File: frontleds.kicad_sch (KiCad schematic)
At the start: 2 parts

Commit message: finished adding front leds
probably works idk
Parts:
- D11, D12: footprint LED_SMD:LED_SK6812_PLCC4_5.0x5.0mm_P3.2mm -> LED_SMD:LED_SK6812B_SIDE_4.0mmx1.5mm
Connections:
- net +5V: now also D11.2 (VDD), D12.2 (VDD); no longer D11.3 (VDD), D12.3 (VDD)
- net GND: now also D11.4 (GND), D12.4 (GND); no longer D11.1 (VSS), D12.1 (VSS)
- net GPIO12: now also D11.1 (DIN); no longer D11.2 (DIN)
- new net: D11.3 (DOUT), D12.1 (DIN)
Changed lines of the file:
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@@
+	)
+	(symbol
+		(lib_id "LED:SK6812B")
+		(at 55.88 29.21 0)
+		(unit 1)
+		(exclude_from_sim no)
+		(in_bom yes)
+		(on_board yes)
+		(dnp no)
+		(fields_autoplaced yes)
+		(property "Reference" "D12"
+			(at 66.04 22.7898 0)
+			(effects
+				(font
+					(size 1.27 1.27)
+				)
+			)
+		)
+		(property "Value" "SK6812B"
+			(at 66.04 25.3298 0)
+			(effects
+				(font
+					(size 1.27 1.27)
+				)
+			)
+		)
+		(property "Footprint" "LED_SMD:LED_SK6812B_SIDE_4.0mmx1.5mm"
+			(at 55.88 29.21 0)
+			(effects
+				(font
+					(size 1.27 1.27)
+				)
+				(hide yes)
+			)
+		)
+		(property "Datasheet" "https://core-electronics.com.au/attachments/localcontent/4691_SK68XX_SIDE_REV_55747b5a68c.pdf"
+			(at 55.88 10.16 0)
+			(effects
+				(font
+					(size 1.27 1.27)
+				)
+				(hide yes)
+			)
+		)
+		(property "Description" "RGB LED with integrated controller"
+			(at 55.88 7.62 0)
+			(effects
+				(font
+					(size 1.27 1.27)
+				)
+				(hide yes)
+			)
+		)
+		(pin "3"
+		)
+		(pin "1"
+		)
+		(pin "4"
+		)
+		(pin "2"
+		)
+		(instances
+			(project "robot_pcb"
+				(path "/2f56b371-1597-47e1-a48d-b7f69d342f77/f9fd353d-136c-4b1d-af31-404dc5242855"
+					(reference "D12")
+					(unit 1)
+				)
+			)
+		)
 	)
 	(symbol
@@
 	)
 	(symbol
+		(lib_id "power:GND")
+		(at 41.91 39.37 0)
+		(unit 1)
+		(exclude_from_sim no)
+		(in_bom yes)
+		(on_board yes)
+		(dnp no)
+		(fields_autoplaced yes)
+		(property "Reference" "#PWR0121"
+			(at 41.91 45.72 0)
+			(effects
+				(font
+					(size 1.27 1.27)
+				)
+				(hide yes)
+			)
+		)
+		(property "Value" "GND"
+			(at 41.91 44.45 0)
+			(effects
+				(font
+					(size 1.27 1.27)
+				)
+			)
+		)
+		(property "Footprint" ""
+			(at 41.91 39.37 0)
+			(effects
+				(font
+					(size 1.27 1.27)
+				)
+				(hide yes)
+			)
+		)
+		(property "Datasheet" ""
+			(at 41.91 39.37 0)
+			(effects
+				(font
+					(size 1.27 1.27)
+				)
+				(hide yes)
+			)
+		)
+		(property "Description" "Power symbol creates a global label with name \"GND\" , ground"
+			(at 41.91 39.37 0)
+			(effects
+				(font
+					(size 1.27 1.27)
+				)
+				(hide yes)
+			)
+		)
+		(pin "1"
+		)
+		(instances
+			(project ""
+				(path "/2f56b371-1597-47e1-a48d-b7f69d342f77/f9fd353d-136c-4b1d-af31-404dc5242855"
+					(reference "#PWR0121")
+					(unit 1)
+				)
+			)
+		)
+	)
+	(symbol
 		(lib_id "LED:SK6812B")
 		(at 29.21 29.21 0)
@@
 		(fields_autoplaced yes)
 		(property "Reference" "D11"
-			(at 40.64 22.7898 0)
+			(at 39.37 22.7898 0)
 			(effects
 				(font
@@
 		)
 		(property "Value" "SK6812B"
-			(at 40.64 25.3298 0)
-			(effects
-				(font
-					(size 1.27 1.27)
-				)
-			)
-		)
-		(property "Footprint" "LED_SMD:LED_SK6812_PLCC4_5.0x5.0mm_P3.2mm"
-			(at 30.48 36.83 0)
-			(effects
-				(font
-					(size 1.27 1.27)
-				)
-				(justify left top)
+			(at 39.37 25.3298 0)
+			(effects
+				(font
+					(size 1.27 1.27)
+				)
+			)
+		)
+		(property "Footprint" "LED_SMD:LED_SK6812B_SIDE_4.0mmx1.5mm"
+			(at 29.21 29.21 0)
+			(effects
+				(font
+					(size 1.27 1.27)
+				)
 				(hide yes)
 			)
 		)
 		(property "Datasheet" "https://core-electronics.com.au/attachments/localcontent/4691_SK68XX_SIDE_REV_55747b5a68c.pdf"
-			(at 31.75 38.735 0)
-			(effects
-				(font
-					(size 1.27 1.27)
-				)
-				(justify left top)
-				(hide yes)
-			)
-		)
-		(property "Description" "Side-light RGB LED with integrated controller"
-			(at 29.21 29.21 0)
-			(effects
-				(font
-					(size 1.27 1.27)
-				)
-				(hide yes)
-			)
+			(at 29.21 10.16 0)
+			(effects
+				(font
+					(size 1.27 1.27)
+				)
+				(hide yes)
+			)
+		)
+		(property "Description" "RGB LED with integrated controller"
+			(at 29.21 7.62 0)
+			(effects
+				(font
+					(size 1.27 1.27)
+				)
+				(hide yes)
+			)
+		)
+		(pin "3"
+		)
+		(pin "1"
+		)
+		(pin "4"
 		)
 		(pin "2"
 		)
-		(pin "1"
-		)
-		(pin "4"
-		)
-		(pin "3"
-		)
 		(instances
 			(project ""
@@
 					(unit 1)
 				)
-			)
-		)
-	)
-	(symbol
-		(lib_id "power:GND")
-		(at 41.91 39.37 0)
-		(unit 1)
-		(exclude_from_sim no)
-		(in_bom yes)
-		(on_board yes)
-		(dnp no)
-		(fields_autoplaced yes)
-		(property "Reference" "#PWR0121"
-			(at 41.91 45.72 0)
-			(effects
-				(font
-					(size 1.27 1.27)
-				)
-				(hide yes)
-			)
-		)
-		(property "Value" "GND"
-			(at 41.91 44.45 0)
-			(effects
-				(font
-					(size 1.27 1.27)
-				)
-			)
-		)
-		(property "Footprint" ""
-			(at 41.91 39.37 0)
-			(effects
-				(font
-					(size 1.27 1.27)
-				)
-				(hide yes)
-			)
-		)
-		(property "Datasheet" ""
-			(at 41.91 39.37 0)
-			(effects
-				(font
-					(size 1.27 1.27)
-				)
-				(hide yes)
-			)
-		)
-		(property "Description" "Power symbol creates a global label with name \"GND\" , ground"
-			(at 41.91 39.37 0)
-			(effects
-				(font
-					(size 1.27 1.27)
-				)
-				(hide yes)
-			)
-		)
-		(pin "1"
-		)
-		(instances
-			(project ""
-				(path "/2f56b371-1597-47e1-a48d-b7f69d342f77/f9fd353d-136c-4b1d-af31-404dc5242855"
-					(reference "#PWR0121")
-					(unit 1)
-				)
-			)
-		)
-	)
-	(symbol
-		(lib_id "LED:SK6812B")
-		(at 55.88 29.21 0)
-		(unit 1)
-		(exclude_from_sim no)
-		(in_bom yes)
-		(on_board yes)
-		(dnp no)
-		(fields_autoplaced yes)
-		(property "Reference" "D12"
-			(at 67.31 22.7898 0)
-			(effects
-				(font
-					(size 1.27 1.27)
-				)
-			)
-		)
-		(property "Value" "SK6812B"
-			(at 67.31 25.3298 0)
-			(effects
-				(font
-					(size 1.27 1.27)
-				)
-			)
-		)
-		(property "Footprint" "LED_SMD:LED_SK6812_PLCC4_5.0x5.0mm_P3.2mm"
-			(at 57.15 36.83 0)
-			(effects
-				(font
-					(size 1.27 1.27)
-				)
-				(justify left top)
-				(hide yes)
-			)
-		)
-		(property "Datasheet" "https://core-electronics.com.au/attachments/localcontent/4691_SK68XX_SIDE_REV_55747b5a68c.pdf"
-			(at 58.42 38.735 0)
-			(effects
-				(font
-					(size 1.27 1.27)
-				)
-				(justify left top)
-				(hide yes)
-			)
-		)
-		(property "Description" "Side-light RGB LED with integrated controller"
-			(at 55.88 29.21 0)
-			(effects
-				(font
-					(size 1.27 1.27)
-				)
-				(hide yes)
-			)
-		)
-		(pin "2"
-		)
-		(pin "1"
-		)
-		(pin "4"
-		)
-		(pin "3"
-		)
-		(instances
-			(project "robot_pcb"
-				(path "/2f56b371-1597-47e1-a48d-b7f69d342f77/f9fd353d-136c-4b1d-af31-404dc5242855"
-					(reference "D12")
-					(unit 1)
-				)

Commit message: send help
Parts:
- removed D11, D12: SK6812B, LED_SMD:LED_SK6812B_SIDE_4.0mmx1.5mm, symbol LED:SK6812B
- added J12, J13: Conn_01x02_Socket, Connector:JWT_A3963_1x02_P3.96mm_Vertical, symbol Connector:Conn_01x02_Socket
- added R54, R55: 8, Resistor_SMD:R_0402_1005Metric, symbol Device:R
- added U18: DMG2305UX-7, Package_TO_SOT_SMD:TSOT-23, symbol Transistor_FET:DMG2305UX-7
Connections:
- net GND: now also J12.2 (Pin_2), J13.2 (Pin_2)
- net GPIO12: now also U18.1 (G)
- new net: R54.1, R55.1
- new net +12V: U18.2 (S)
- new net LED1: J12.1 (Pin_1), R54.2
- new net LED2: J13.1 (Pin_1), R55.2
- no-connect marks 1 -> 0

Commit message: more stuff with switches n things
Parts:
- R54, R55: value 8 -> 10
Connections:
- net at R54.1, R55.1: now also U18.3 (D)
- net LED1: no longer names the net of J12.1 (Pin_1), R54.2
- net LED2: no longer names the net of J13.1 (Pin_1), R55.2
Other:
- moved on the sheet: J12, J13, R54, R55, U18

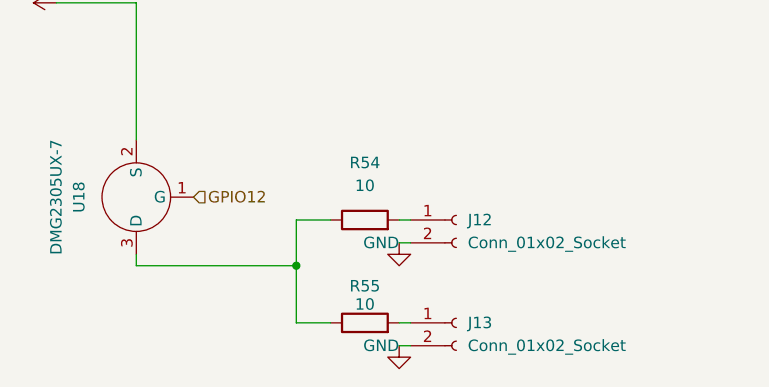
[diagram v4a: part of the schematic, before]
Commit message: added labels to everything
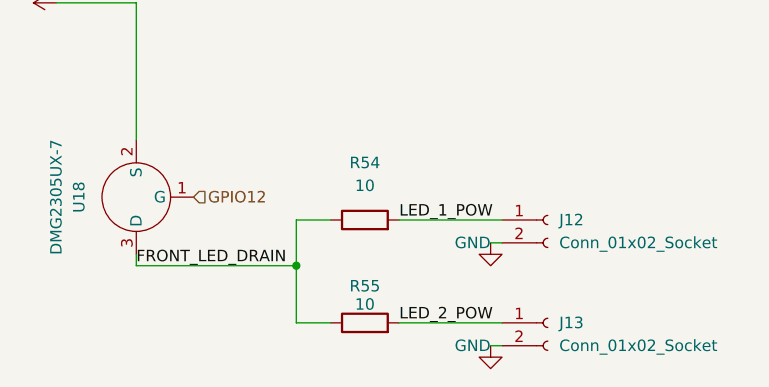
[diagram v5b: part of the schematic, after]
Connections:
- net FRONT_LED_DRAIN: now reaches R54.1, R55.1, U18.3 (D)
- net LED_1_POW: now reaches J12.1 (Pin_1), R54.2
- net LED_2_POW: now reaches J13.1 (Pin_1), R55.2
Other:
- moved on the sheet: J12, J13
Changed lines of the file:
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@@
 	(wire
 		(pts
-			(xy 82.55 63.5) (xy 83.82 63.5)
-		)
-		(stroke
-			(width 0)
-			(type default)
-		)
-	)
-	(wire
-		(pts
-			(xy 82.55 60.96) (xy 83.82 60.96)
+			(xy 92.71 63.5) (xy 93.98 63.5)
 		)
 		(stroke
@@
 	(wire
 		(pts
-			(xy 82.55 52.07) (xy 83.82 52.07)
+			(xy 82.55 60.96) (xy 93.98 60.96)
+		)
+		(stroke
+			(width 0)
+			(type default)
+		)
+	)
+	(wire
+		(pts
+			(xy 92.71 52.07) (xy 93.98 52.07)
 		)
 		(stroke
@@
 	(wire
 		(pts
-			(xy 82.55 49.53) (xy 83.82 49.53)
+			(xy 82.55 49.53) (xy 93.98 49.53)
 		)
 		(stroke
@@
 			(width 0)
 			(type default)
+		)
+	)
+	(label "LED_2_POW"
+		(at 82.55 60.96 0)
+		(effects
+			(font
+				(size 1.27 1.27)
+			)
+			(justify left bottom)
+		)
+	)
+	(label "FRONT_LED_DRAIN"
+		(at 53.34 54.61 0)
+		(effects
+			(font
+				(size 1.27 1.27)
+			)
+			(justify left bottom)
+		)
+	)
+	(label "LED_1_POW"
+		(at 82.55 49.53 0)
+		(effects
+			(font
+				(size 1.27 1.27)
+			)
+			(justify left bottom)
 		)
 	)
@@
 	(symbol
 		(lib_id "power:GND")
-		(at 82.55 63.5 0)
+		(at 92.71 63.5 0)
 		(unit 1)
 		(exclude_from_sim no)
@@
 		(dnp no)
 		(property "Reference" "#PWR0124"
-			(at 82.55 69.85 0)
+			(at 92.71 69.85 0)
 			(effects
 				(font
@@
 		)
 		(property "Value" "GND"
-			(at 82.55 63.5 0)
+			(at 92.71 63.5 0)
 			(effects
 				(font
@@
 		)
 		(property "Footprint" ""
-			(at 82.55 63.5 0)
+			(at 92.71 63.5 0)
 			(effects
 				(font
@@
 		)
 		(property "Datasheet" ""
-			(at 82.55 63.5 0)
+			(at 92.71 63.5 0)
 			(effects
 				(font
@@
 		)
 		(property "Description" "Power symbol creates a global label with name \"GND\" , ground"
-			(at 82.55 63.5 0)
+			(at 92.71 63.5 0)
 			(effects
 				(font
@@
 	(symbol
 		(lib_id "Connector:Conn_01x02_Socket")
-		(at 88.9 49.53 0)
+		(at 99.06 49.53 0)
 		(unit 1)
 		(exclude_from_sim no)
@@
 		(fields_autoplaced yes)
 		(property "Reference" "J12"
-			(at 90.17 49.5299 0)
+			(at 100.33 49.5299 0)
 			(effects
 				(font
@@
 		)
 		(property "Value" "Conn_01x02_Socket"
-			(at 90.17 52.0699 0)
+			(at 100.33 52.0699 0)
 			(effects
 				(font
@@
 		)
 		(property "Footprint" "Connector:JWT_A3963_1x02_P3.96mm_Vertical"
-			(at 88.9 49.53 0)
+			(at 99.06 49.53 0)
 			(effects
 				(font
@@
 		)
 		(property "Datasheet" "~"
-			(at 88.9 49.53 0)
+			(at 99.06 49.53 0)
 			(effects
 				(font
@@
 		)
 		(property "Description" "Generic connector, single row, 01x02, script generated"
-			(at 88.9 49.53 0)
+			(at 99.06 49.53 0)
 			(effects
 				(font
@@
 	(symbol
 		(lib_id "power:GND")
-		(at 82.55 52.07 0)
+		(at 92.71 52.07 0)
 		(unit 1)
 		(exclude_from_sim no)
@@
 		(dnp no)
 		(property "Reference" "#PWR0121"
-			(at 82.55 58.42 0)
+			(at 92.71 58.42 0)
 			(effects
 				(font
@@
 		)
 		(property "Value" "GND"
-			(at 82.55 52.07 0)
+			(at 92.71 52.07 0)
 			(effects
 				(font
@@
 		)
 		(property "Footprint" ""
-			(at 82.55 52.07 0)
+			(at 92.71 52.07 0)
 			(effects
 				(font
@@
 		)
 		(property "Datasheet" ""
-			(at 82.55 52.07 0)
+			(at 92.71 52.07 0)
 			(effects
 				(font
@@
 		)
 		(property "Description" "Power symbol creates a global label with name \"GND\" , ground"
-			(at 82.55 52.07 0)
+			(at 92.71 52.07 0)
 			(effects
 				(font
@@
 	(symbol
 		(lib_id "Connector:Conn_01x02_Socket")
-		(at 88.9 60.96 0)
+		(at 99.06 60.96 0)
 		(unit 1)
 		(exclude_from_sim no)
@@
 		(fields_autoplaced yes)
 		(property "Reference" "J13"
-			(at 90.17 60.9599 0)
+			(at 100.33 60.9599 0)
 			(effects
 				(font
@@
 		)
 		(property "Value" "Conn_01x02_Socket"
-			(at 90.17 63.4999 0)
+			(at 100.33 63.4999 0)
 			(effects
 				(font
@@
 		)
 		(property "Footprint" "Connector:JWT_A3963_1x02_P3.96mm_Vertical"
-			(at 88.9 60.96 0)
+			(at 99.06 60.96 0)
 			(effects
 				(font
@@
 		)
 		(property "Datasheet" "~"
-			(at 88.9 60.96 0)
+			(at 99.06 60.96 0)
 			(effects
 				(font
@@
 		)
 		(property "Description" "Generic connector, single row, 01x02, script generated"
-			(at 88.9 60.96 0)
-			(effects
-				(font
+			(at 99.06 60.96 0)
+			(effects
+				(font

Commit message: more lcsc part labels for non generic components
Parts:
- U18: LCSC (none) -> C150470
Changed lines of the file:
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@@
 			)
 		)
-		(property "LCSC" ""
+		(property "LCSC" "C150470"
 			(at 53.34 46.99 90)
 			(effects

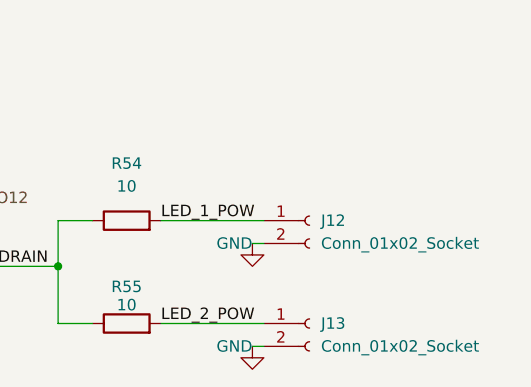
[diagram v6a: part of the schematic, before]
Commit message: Updated edge cuts and drawings from earlier fusion changes and moved traces accordingly
Also fixed jst connectors
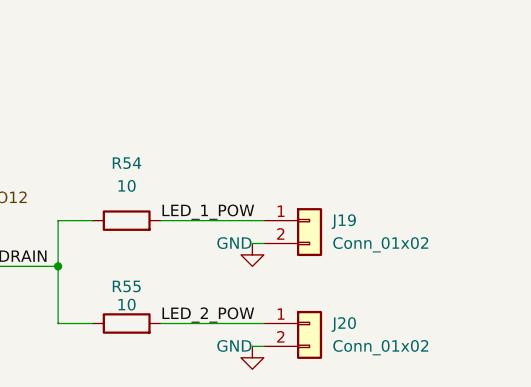
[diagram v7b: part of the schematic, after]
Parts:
- removed J12, J13: Conn_01x02_Socket, Connector:JWT_A3963_1x02_P3.96mm_Vertical, symbol Connector:Conn_01x02_Socket
- added J19, J20: Conn_01x02, Connector_JST:JST_PH_B2B-PH-K_1x02_P2.00mm_Vertical, symbol Connector_Generic:Conn_01x02
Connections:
- net GND: now also J19.2 (Pin_2), J20.2 (Pin_2)
- net LED_1_POW: now also J19.1 (Pin_1)
- net LED_2_POW: now also J20.1 (Pin_1)
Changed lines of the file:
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@@
-	)
-	(symbol
-		(lib_id "Connector:Conn_01x02_Socket")
-		(at 99.06 49.53 0)
-		(unit 1)
-		(exclude_from_sim no)
-		(in_bom yes)
-		(on_board yes)
-		(dnp no)
-		(fields_autoplaced yes)
-		(property "Reference" "J12"
-			(at 100.33 49.5299 0)
-			(effects
-				(font
-					(size 1.27 1.27)
-				)
-				(justify left)
-			)
-		)
-		(property "Value" "Conn_01x02_Socket"
-			(at 100.33 52.0699 0)
-			(effects
-				(font
-					(size 1.27 1.27)
-				)
-				(justify left)
-			)
-		)
-		(property "Footprint" "Connector:JWT_A3963_1x02_P3.96mm_Vertical"
-			(at 99.06 49.53 0)
-			(effects
-				(font
-					(size 1.27 1.27)
-				)
-				(hide yes)
-			)
-		)
-		(property "Datasheet" "~"
-			(at 99.06 49.53 0)
-			(effects
-				(font
-					(size 1.27 1.27)
-				)
-				(hide yes)
-			)
-		)
-		(property "Description" "Generic connector, single row, 01x02, script generated"
-			(at 99.06 49.53 0)
-			(effects
-				(font
-					(size 1.27 1.27)
-				)
-				(hide yes)
-			)
-		)
-		(pin "2"
-		)
-		(pin "1"
-		)
-		(instances
-			(project ""
-				(path "/2f56b371-1597-47e1-a48d-b7f69d342f77/f9fd353d-136c-4b1d-af31-404dc5242855"
-					(reference "J12")
-					(unit 1)
-				)
-			)
-		)
 	)
 	(symbol
@@
 				(path "/2f56b371-1597-47e1-a48d-b7f69d342f77/f9fd353d-136c-4b1d-af31-404dc5242855"
 					(reference "#PWR0121")
-					(unit 1)
-				)
-			)
-		)
-	)
-	(symbol
-		(lib_id "Connector:Conn_01x02_Socket")
-		(at 99.06 60.96 0)
-		(unit 1)
-		(exclude_from_sim no)
-		(in_bom yes)
-		(on_board yes)
-		(dnp no)
-		(fields_autoplaced yes)
-		(property "Reference" "J13"
-			(at 100.33 60.9599 0)
-			(effects
-				(font
-					(size 1.27 1.27)
-				)
-				(justify left)
-			)
-		)
-		(property "Value" "Conn_01x02_Socket"
-			(at 100.33 63.4999 0)
-			(effects
-				(font
-					(size 1.27 1.27)
-				)
-				(justify left)
-			)
-		)
-		(property "Footprint" "Connector:JWT_A3963_1x02_P3.96mm_Vertical"
-			(at 99.06 60.96 0)
-			(effects
-				(font
-					(size 1.27 1.27)
-				)
-				(hide yes)
-			)
-		)
-		(property "Datasheet" "~"
-			(at 99.06 60.96 0)
-			(effects
-				(font
-					(size 1.27 1.27)
-				)
-				(hide yes)
-			)
-		)
-		(property "Description" "Generic connector, single row, 01x02, script generated"
-			(at 99.06 60.96 0)
-			(effects
-				(font
-					(size 1.27 1.27)
-				)
-				(hide yes)
-			)
-		)
-		(pin "2"
-		)
-		(pin "1"
-		)
-		(instances
-			(project "robot_pcb"
-				(path "/2f56b371-1597-47e1-a48d-b7f69d342f77/f9fd353d-136c-4b1d-af31-404dc5242855"
-					(reference "J13")
 					(unit 1)
 				)
@@
 					(unit 1)
 				)
+			)
+		)
+	)
+	(symbol
+		(lib_id "Connector_Generic:Conn_01x02")
+		(at 99.06 60.96 0)
+		(unit 1)
+		(exclude_from_sim no)
+		(in_bom yes)
+		(on_board yes)
+		(dnp no)
+		(fields_autoplaced yes)
+		(property "Reference" "J20"
+			(at 101.6 60.9599 0)
+			(effects
+				(font
+					(size 1.27 1.27)
+				)
+				(justify left)
+			)
+		)
+		(property "Value" "Conn_01x02"
+			(at 101.6 63.4999 0)
+			(effects
+				(font
+					(size 1.27 1.27)
+				)
+				(justify left)
+			)
+		)
+		(property "Footprint" "Connector_JST:JST_PH_B2B-PH-K_1x02_P2.00mm_Vertical"
+			(at 99.06 60.96 0)
+			(effects
+				(font
+					(size 1.27 1.27)
+				)
+				(hide yes)
+			)
+		)
+		(property "Datasheet" "~"
+			(at 99.06 60.96 0)
+			(effects
+				(font
+					(size 1.27 1.27)
+				)
+				(hide yes)
+			)
+		)
+		(property "Description" "Generic connector, single row, 01x02, script generated (kicad-library-utils/schlib/autogen/connector/)"
+			(at 99.06 60.96 0)
+			(effects
+				(font
+					(size 1.27 1.27)
+				)
+				(hide yes)
+			)
+		)
+		(pin "2"
+		)
+		(pin "1"
+		)
+		(instances
+			(project "robot_pcb"
+				(path "/2f56b371-1597-47e1-a48d-b7f69d342f77/f9fd353d-136c-4b1d-af31-404dc5242855"
+					(reference "J20")
+					(unit 1)
+				)
+			)
+		)
+	)
+	(symbol
+		(lib_id "Connector_Generic:Conn_01x02")
+		(at 99.06 49.53 0)
+		(unit 1)
+		(exclude_from_sim no)
+		(in_bom yes)
+		(on_board yes)
+		(dnp no)
+		(fields_autoplaced yes)
+		(property "Reference" "J19"
+			(at 101.6 49.5299 0)
+			(effects
+				(font
+					(size 1.27 1.27)
+				)
+				(justify left)
+			)
+		)
+		(property "Value" "Conn_01x02"
+			(at 101.6 52.0699 0)
+			(effects
+				(font
+					(size 1.27 1.27)
+				)
+				(justify left)
+			)
+		)
+		(property "Footprint" "Connector_JST:JST_PH_B2B-PH-K_1x02_P2.00mm_Vertical"
+			(at 99.06 49.53 0)
+			(effects
+				(font
+					(size 1.27 1.27)
+				)
+				(hide yes)
+			)
+		)
+		(property "Datasheet" "~"
+			(at 99.06 49.53 0)
+			(effects
+				(font
+					(size 1.27 1.27)
+				)
+				(hide yes)
+			)
+		)
+		(property "Description" "Generic connector, single row, 01x02, script generated (kicad-library-utils/schlib/autogen/connector/)"
+			(at 99.06 49.53 0)
+			(effects
+				(font
+					(size 1.27 1.27)
+				)
+				(hide yes)
+			)
+		)
+		(pin "2"
+		)
+		(pin "1"
+		)
+		(instances
+			(project ""
+				(path "/2f56b371-1597-47e1-a48d-b7f69d342f77/f9fd353d-136c-4b1d-af31-404dc5242855"
+					(reference "J19")
+					(unit 1)
+				)
